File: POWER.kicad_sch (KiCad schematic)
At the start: 55 parts, among them J1 JST-PH 2-pin, U11 MAX17048G+, U13 BQ25895RTW, U23 LT3154AV#TRPBF, U24 TPS61023DRLR, U25 TPS2553DBVR

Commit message: finished annotation
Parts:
- removed U24: TPS61023DRLR, TPS61023:SOT563-ORI, symbol TPS61023DRLR:TPS61023DRLR
- added C21: 22u, symbol Device:C
- added U49: TPS61022, Package_DFN_QFN:Texas_RWU0007A_VQFN-7_2x2mm_P0.5mm, symbol Converter_DCDC:TPS61022
- renumbered C7 to C1, C14 to C10, C9 to C11, C15 to C12, C16 to C13, C12 to C14, C10 to C15, C8 to C16, C20 to C17, C21 to C18, C18 to C19, C5 to C2, C19 to C20, C17 to C22, C1 to C4, C2 to C5, C4 to C7, C11 to C8, C13 to C9, R5 to R1, R9 to R10, R6 to R11, R16 to R12, R17 to R13, R15 to R14, R14 to R15, R12 to R16, R13 to R17, R1 to R2, R4 to R3, R3 to R4, R2 to R5, R10 to R6, R11 to R7, R7 to R8, R8 to R9
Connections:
- net +5V_SYS: now also C21.2, U49.3 (VOUT)
- net BOOST_5V_EN: now also U49.5 (EN)
- net GND: now also C21.1, U49.1 (GND)
- net VSYS: now also U49.6 (MODE), U49.7 (VIN)
- net BST5V_FB renamed BOOST5V_FB
- net BOOST5V_FB: now also U49.4 (FB)
- net BST5V_SW renamed BOOST5V_SW
- net BOOST5V_SW: now also U49.2 (SW)
- net CHG_USB_DM: no longer names the net of U13.3 (D-)
- net CHG_USB_DP: no longer names the net of U13.2 (D+)
- net PMID renamed CHG_PMID
- net REGN renamed CHG_REGN
- net TS renamed CHG_TS
- net USB_ILIM renamed USB_HOST_ILIM
- net USB_MUX_SEL renamed CHG_DSEL_CFG
- no-connect marks 4 -> 6
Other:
- note added: "SWITCHABLE 5 V BOOST REGULATOR - TPS61022 VSYS TO +5V_SYS"
- note removed: "SWITCHABLE 5 V BOOST REGULATOR - TPS61023 VSYS TO +5V_SYS"
- title: (none) -> Power Input, Charging, Battery Monitoring and Regulated Rails
- moved on the sheet: C19, C2, C20, R14

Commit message: finished ANCHOR_DOCK sheet
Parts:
- removed C18: 120u, symbol Device:C
- removed J1: JST-PH 2-pin, symbol Connector_Generic:Conn_01x02
- added BT1: VTC-LP484594 3.7V 2200mAh protected battery pack, symbol Connector_Generic:Conn_01x03
- added C18: 120u, symbol Device:C_Polarized
- added J1: S3B-PH-SM4-TB(LF)(SN), Connector_JST:JST_PH_S3B-PH-SM4-TB_1x03-1MP_P2.00mm_Horizontal, symbol Connector_Generic:Conn_01x03
- C1: footprint (none) -> Capacitor_SMD:C_0603_1608Metric; DISTRIBUTOR_LINK (none) -> https://www.mouser.com/ProductDetail/Murata-Electronics/GRM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; MANUFACTURER (none) -> Murata; MPN (none) -> GRM188R71C105KA12D; Notes (none) -> N/A
- C10, C8, C9: footprint (none) -> Capacitor_SMD:C_1210_3225Metric; DISTRIBUTOR_LINK (none) -> https://www.mouser.com/ProductDetail/Murata-Electronics/GRM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; MANUFACTURER (none) -> Murata; MPN (none) -> GRM32ER71A476KE15L; Notes (none) -> Verify effective capacitance under DC bias.
- C11, C12, C19, C2, C20, C21, C4, C5: footprint (none) -> Capacitor_SMD:C_1206_3216Metric; DISTRIBUTOR_LINK (none) -> https://www.mouser.com/ProductDetail/Murata-Electronics/GRM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; MANUFACTURER (none) -> Murata; MPN (none) -> GRM31CR71A226KE15L; Notes (none) -> Verify effective capacitance under DC bias.
- C13: footprint (none) -> Capacitor_SMD:C_0603_1608Metric; DISTRIBUTOR_LINK (none) -> https://www.mouser.com/ProductDetail/Murata-Electronics/GRM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; MANUFACTURER (none) -> Murata; MPN (none) -> GRM188R71A225KE15D; Notes (none) -> N/A
- C14: footprint (none) -> Capacitor_SMD:C_0603_1608Metric; DISTRIBUTOR_LINK (none) -> https://www.mouser.com/ProductDetail/Murata-Electronics/GRM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; MANUFACTURER (none) -> Murata; MPN (none) -> GRM1885C1H100JA01D; Notes (none) -> N/A
- C15: footprint (none) -> Capacitor_SMD:C_0603_1608Metric; DISTRIBUTOR_LINK (none) -> https://www.mouser.com/ProductDetail/Murata-Electronics/GRM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; MANUFACTURER (none) -> Murata; MPN (none) -> GRM1885C1H102JA01D; Notes (none) -> N/A
- C16, C17: footprint (none) -> Capacitor_SMD:C_0603_1608Metric; DISTRIBUTOR_LINK (none) -> https://www.mouser.com/ProductDetail/Murata-Electronics/GRM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; MANUFACTURER (none) -> Murata; MPN (none) -> GRM188R71C104KA01D; Notes (none) -> N/A
- C22, C6: footprint (none) -> Capacitor_SMD:C_0805_2012Metric; DISTRIBUTOR_LINK (none) -> https://www.mouser.com/ProductDetail/Murata-Electronics/GRM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; MANUFACTURER (none) -> Murata; MPN (none) -> GRM21BR71A106KE51L; Notes (none) -> Verify effective capacitance under DC bias.
- C3: footprint (none) -> Capacitor_SMD:C_0603_1608Metric; DISTRIBUTOR_LINK (none) -> https://www.mouser.com/ProductDetail/Murata-Electronics/GRM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; MANUFACTURER (none) -> Murata; MPN (none) -> GRM188R71C473KA01D; Notes (none) -> N/A
- C7: footprint (none) -> Capacitor_SMD:C_0805_2012Metric; DISTRIBUTOR_LINK (none) -> https://www.mouser.com/ProductDetail/Murata-Electronics/GRM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; MANUFACTURER (none) -> Murata; MPN (none) -> GRM21BR71A475KA73L; Notes (none) -> Verify effective capacitance under DC bias.
- L1: footprint (none) -> Inductor_SMD:L_Wuerth_MAPI-4020; DISTRIBUTOR_LINK (none) -> https://www.mouser.com/ProductDetail/Wurth-Elektronik/74438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; MANUFACTURER (none) -> Wurth Elektronik; MPN (none) -> 74438356022; Notes (none) -> Verify charger thermal and layout.
- L2: footprint (none) -> Inductor_SMD:L_Wuerth_MAPI-4020; DISTRIBUTOR_LINK (none) -> https://www.mouser.com/ProductDetail/Wurth-Elektronik/74438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; MANUFACTURER (none) -> Wurth Elektronik; MPN (none) -> 744383560047HT; Notes (none) -> Verify peak current and switching frequency.
- L3: footprint (none) -> Inductor_SMD:L_Wuerth_HCI-5040; DISTRIBUTOR_LINK (none) -> https://www.mouser.com/ProductDetail/Wurth-Elektronik/74431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; MANUFACTURER (none) -> Wurth Elektronik; MPN (none) -> 744316100; Notes (none) -> Verify boost thermal and layout.
- NT1: DISTRIBUTOR_LINK (none) -> N/A; MANUFACTURER (none) -> PCB feature; MPN (none) -> N/A; Notes (none) -> N/A
- R1, R3: footprint (none) -> Resistor_SMD:R_0603_1608Metric; DISTRIBUTOR_LINK (none) -> https://www.mouser.com/ProductDetail/YAGEO/RC0603FR-0710KL?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; MANUFACTURER (none) -> Yageo; MPN (none) -> RC0603FR-0710KL; Notes (none) -> N/A
- R10: value 32.2k -> 32k4; footprint (none) -> Resistor_SMD:R_0603_1608Metric; DISTRIBUTOR_LINK (none) -> https://www.mouser.co.il/en/ProductDetail/YAGEO/RC0603FR-07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; MANUFACTURER (none) -> Yageo; MPN (none) -> RC0603FR-0732K4L
- R11: footprint (none) -> Resistor_SMD:R_0603_1608Metric; DISTRIBUTOR_LINK (none) -> https://www.mouser.com/ProductDetail/YAGEO/RC0603FR-0740K2L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; MANUFACTURER (none) -> Yageo; MPN (none) -> RC0603FR-0740K2L; Notes (none) -> N/A
- R12, R13, R15, R17, R7, R9: footprint (none) -> Resistor_SMD:R_0603_1608Metric; DISTRIBUTOR_LINK (none) -> https://www.mouser.com/ProductDetail/YAGEO/RC0603FR-07100KL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; MANUFACTURER (none) -> Yageo; MPN (none) -> RC0603FR-07100KL; Notes (none) -> N/A
- R14: footprint (none) -> Resistor_SMD:R_0603_1608Metric; DISTRIBUTOR_LINK (none) -> https://www.mouser.com/ProductDetail/YAGEO/RC0603FR-0743K2L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; MANUFACTURER (none) -> Yageo; MPN (none) -> RC0603FR-0743K2L; Notes (none) -> N/A
- R16: footprint (none) -> Resistor_SMD:R_0603_1608Metric; DISTRIBUTOR_LINK (none) -> https://www.mouser.com/ProductDetail/YAGEO/RC0603FR-07732KL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; MANUFACTURER (none) -> Yageo; MPN (none) -> RC0603FR-07732KL; Notes (none) -> N/A
- R2: value 260R -> 261R; footprint (none) -> Resistor_SMD:R_0603_1608Metric; DISTRIBUTOR_LINK (none) -> https://www.mouser.com/en/ProductDetail/YAGEO/AF0603FR-0726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; MANUFACTURER (none) -> Yageo; MPN (none) -> AF0603FR-07261RL
- R4: value 10k -> 5k23; footprint (none) -> Resistor_SMD:R_0603_1608Metric; DISTRIBUTOR_LINK (none) -> https://eu.mouser.com/en/ProductDetail/YAGEO/RC0603FR-075K2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; MANUFACTURER (none) -> Yageo; MPN (none) -> RC0603FR-075K23L; Notes (none) -> N/A
- R5: value 10k -> 30k1; footprint (none) -> Resistor_SMD:R_0603_1608Metric; DISTRIBUTOR_LINK (none) -> https://eu.mouser.com/en/ProductDetail/YAGEO/RC0603FR-0730K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; MANUFACTURER (none) -> Yageo; MPN (none) -> RC0603FR-0730K1L; Notes (none) -> N/A
- R6: footprint (none) -> Resistor_SMD:R_0603_1608Metric; DISTRIBUTOR_LINK (none) -> https://www.mouser.com/ProductDetail/YAGEO/RC0603FR-07121KL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; MANUFACTURER (none) -> Yageo; MPN (none) -> RC0603FR-07121KL; Notes (none) -> N/A
- R8: footprint (none) -> Resistor_SMD:R_0603_1608Metric; DISTRIBUTOR_LINK (none) -> https://www.mouser.com/ProductDetail/YAGEO/RC0603FR-07232KL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; MANUFACTURER (none) -> Yageo; MPN (none) -> RC0603FR-07232KL; Notes (none) -> N/A
- TP1, TP2, TP3, TP4, TP5, TP6, TP7: footprint (none) -> TestPoint:TestPoint_Pad_D1.5mm; DISTRIBUTOR_LINK (none) -> N/A; MANUFACTURER (none) -> PCB feature; MPN (none) -> N/A; Notes (none) -> N/A; now left out of the parts list
- U11: DISTRIBUTOR_LINK (none) -> https://www.mouser.com/ProductDetail/Analog-Devices-Maxim-I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; MANUFACTURER (none) -> Analog Devices; MPN (none) -> MAX17048G+T10; Notes (none) -> Confirm battery profile assumptions.
- U13: DISTRIBUTOR_LINK (none) -> https://www.mouser.com/ProductDetail/Texas-Instruments/BQ25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; MANUFACTURER (none) -> Texas Instruments; MPN (none) -> BQ25895RTWR; Notes (none) -> Assembly: exposed pad, thermal vias and X-ray.
- U23: DISTRIBUTOR_LINK (none) -> https://www.mouser.com/ProductDetail/Analog-Devices/LT3154A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; MPN (none) -> LT3154AV#TRPBF; Notes (none) -> SOURCING: non-stocked/long lead; obtain PCBWay quote.
- U25: DISTRIBUTOR_LINK (none) -> https://www.mouser.com/ProductDetail/Texas-Instruments/TPS2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; MANUFACTURER (none) -> Texas Instruments; MPN (none) -> TPS2553DBVR; Notes (none) -> N/A
- U49: DISTRIBUTOR_LINK (none) -> https://www.mouser.com/ProductDetail/Texas-Instruments/TPS6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; MANUFACTURER (none) -> Texas Instruments; MPN (none) -> TPS61022RWUR; Notes (none) -> Assembly: EP ground/X-ray; verify peak current/thermal.
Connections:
- net CHG_TS: now also J1.2 (Pin_2)
- net GND: now also C18.2, J1.3 (Pin_3)
- net VBAT: now also J1.1 (Pin_1)
- net VBUS_HOST: now also C18.1
- no-connect marks 6 -> 9

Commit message: the schematic is finished
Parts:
- R10, R2: Notes (none) -> N/A
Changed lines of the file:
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@@
 			)
 		)
-		(property "Notes" ""
+		(property "Notes" "N/A"
 			(at 35.56 69.85 90)
 			(hide yes)
@@
 			)
 		)
-		(property "Notes" ""
+		(property "Notes" "N/A"
 			(at 38.1 168.91 0)
 			(hide yes)

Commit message: finished schematic phase
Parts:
- C18: footprint (none) -> FOBtool_Custom:CP_Panasonic_EEF-TX_7.3x4.3mm
- NT1: footprint (none) -> FOBtool_Custom:NetTie_2_SMD_3.0mm_Current
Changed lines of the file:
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@@
 		(in_bom no)
 		(on_board yes)
-		(in_pos_files yes)
+		(in_pos_files no)
 		(dnp no)
 		(fields_autoplaced yes)
@@
 			)
 		)
-		(property "Footprint" ""
+		(property "Footprint" "FOBtool_Custom:NetTie_2_SMD_3.0mm_Current"
 			(at 33.02 86.36 0)
 			(hide yes)
@@
 			)
 		)
-		(property "Footprint" ""
+		(property "Footprint" "FOBtool_Custom:CP_Panasonic_EEF-TX_7.3x4.3mm"
 			(at 254.9652 88.9 0)
 			(hide yes)

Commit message: adding 3d models
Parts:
- J1: symbol Connector_Generic:Conn_01x03 -> FOBtool_Custom:JST_PH_3Pin_MP
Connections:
- no-connect marks 9 -> 10
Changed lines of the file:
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@@
 	)
 	(no_connect
+		(at 123.19 83.82)
+	)
+	(no_connect
 		(at 53.34 64.77)
 	)
@@
 	)
 	(symbol
-		(lib_id "Connector_Generic:Conn_01x03")
+		(lib_id "FOBtool_Custom:JST_PH_3Pin_MP")
 		(at 118.11 81.28 0)
 		(unit 1)
@@
 		(pin "2"
 		)
+		(pin "MP"
+		)
 		(instances

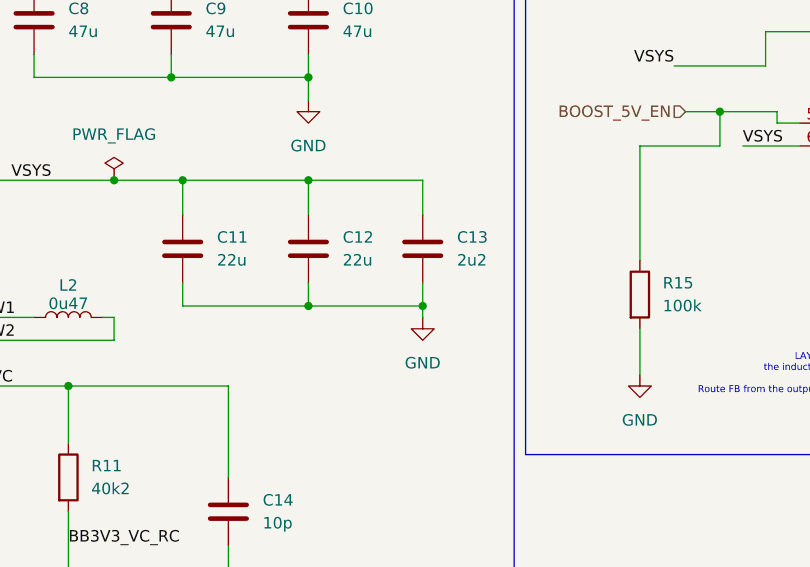
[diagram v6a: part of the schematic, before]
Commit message: changiong bootsel buttom in rp
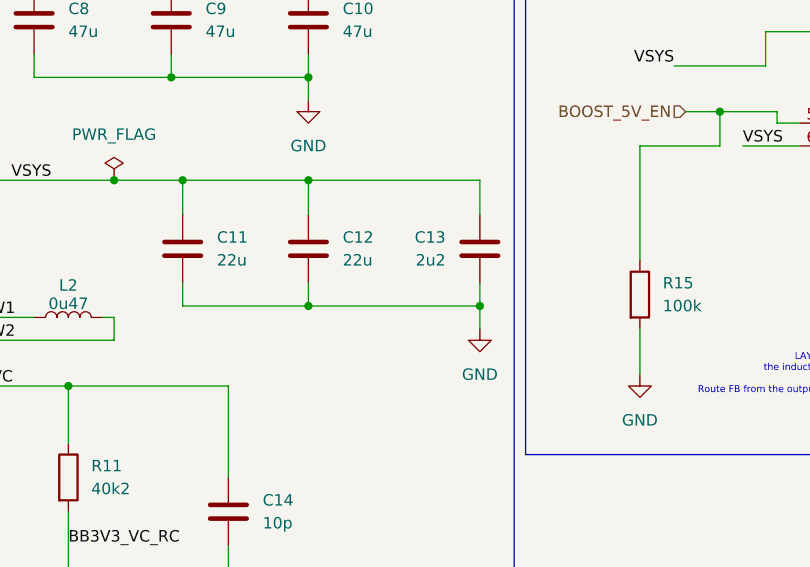
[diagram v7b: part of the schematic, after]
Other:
- moved on the sheet: C13
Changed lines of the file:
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@@
 	)
 	(junction
-		(at 140.97 148.59)
+		(at 140.97 134.62)
 		(diameter 0)
 		(color 0 0 0 0)
@@
 	)
 	(junction
+		(at 160.02 148.59)
+		(diameter 0)
+		(color 0 0 0 0)
+	)
+	(junction
 		(at 242.57 105.41)
 		(diameter 0)
@@
 	)
 	(junction
-		(at 153.67 148.59)
-		(diameter 0)
-		(color 0 0 0 0)
-	)
-	(junction
 		(at 99.06 134.62)
 		(diameter 0)
@@
 	)
 	(junction
-		(at 224.79 24.13)
+		(at 140.97 148.59)
 		(diameter 0)
 		(color 0 0 0 0)
 	)
 	(junction
-		(at 119.38 134.62)
+		(at 224.79 24.13)
 		(diameter 0)
 		(color 0 0 0 0)
 	)
 	(junction
-		(at 129.54 59.69)
+		(at 119.38 134.62)
 		(diameter 0)
 		(color 0 0 0 0)
 	)
 	(junction
-		(at 20.32 162.56)
+		(at 129.54 59.69)
 		(diameter 0)
 		(color 0 0 0 0)
 	)
 	(junction
-		(at 140.97 134.62)
+		(at 20.32 162.56)
 		(diameter 0)
 		(color 0 0 0 0)
@@
 	(wire
 		(pts
-			(xy 153.67 148.59) (xy 140.97 148.59)
+			(xy 140.97 148.59) (xy 160.02 148.59)
 		)
 		(stroke
@@
 	(wire
 		(pts
-			(xy 153.67 148.59) (xy 153.67 149.86)
+			(xy 160.02 148.59) (xy 160.02 151.13)
 		)
 		(stroke
@@
 	(wire
 		(pts
-			(xy 153.67 146.05) (xy 153.67 148.59)
+			(xy 160.02 146.05) (xy 160.02 148.59)
 		)
 		(stroke
@@
 	(wire
 		(pts
-			(xy 153.67 138.43) (xy 153.67 134.62)
+			(xy 160.02 138.43) (xy 160.02 134.62)
 		)
 		(stroke
@@
 	(wire
 		(pts
-			(xy 140.97 134.62) (xy 153.67 134.62)
+			(xy 140.97 134.62) (xy 160.02 134.62)
 		)
 		(stroke
@@
 	(symbol
 		(lib_id "Device:C")
-		(at 153.67 142.24 0)
+		(at 160.02 142.24 0)
+		(mirror y)
 		(unit 1)
 		(body_style 1)
@@
 		(in_pos_files yes)
 		(dnp no)
-		(fields_autoplaced yes)
 		(property "Reference" "C13"
-			(at 157.48 140.9699 0)
+			(at 156.21 140.9699 0)
 			(show_name no)
 			(do_not_autoplace no)
@@
 		)
 		(property "Value" "2u2"
-			(at 157.48 143.5099 0)
+			(at 156.21 143.5099 0)
 			(show_name no)
 			(do_not_autoplace no)
@@
 		)
 		(property "Footprint" "Capacitor_SMD:C_0603_1608Metric"
-			(at 154.6352 146.05 0)
+			(at 159.0548 146.05 0)
 			(hide yes)
 			(show_name no)
@@
 		)
 		(property "Datasheet" "https://pim.murata.com/en-global/pim/details/?partNum=GRM188R71A225KE15D"
-			(at 153.67 142.24 0)
+			(at 160.02 142.24 0)
 			(hide yes)
 			(show_name no)
@@
 		)
 		(property "Description" "Unpolarized capacitor"
-			(at 153.67 142.24 0)
+			(at 160.02 142.24 0)
 			(hide yes)
 			(show_name no)
@@
 		)
 		(property "DISTRIBUTOR_LINK" "https://www.mouser.com/ProductDetail/Murata-Electronics/GRM188R71A225KE15D?qs=FI%2F1jqMWe7rgTInCPAq47w%3D%3D"
-			(at 153.67 142.24 0)
+			(at 160.02 142.24 0)
 			(hide yes)
 			(show_name no)
@@
 		)
 		(property "MPN" "GRM188R71A225KE15D"
-			(at 153.67 142.24 0)
+			(at 160.02 142.24 0)
 			(hide yes)
 			(show_name no)
@@
 		)
 		(property "KLC_S3.3" ""
-			(at 153.67 142.24 0)
+			(at 160.02 142.24 0)
 			(hide yes)
 			(show_name no)
@@
 		)
 		(property "KLC_S4.1" ""
-			(at 153.67 142.24 0)
+			(at 160.02 142.24 0)
 			(hide yes)
 			(show_name no)
@@
 		)
 		(property "KLC_S4.2_DVDD" ""
-			(at 153.67 142.24 0)
+			(at 160.02 142.24 0)
 			(hide yes)
 			(show_name no)
@@
 		)
 		(property "KLC_S4.2_VREG_LX" ""
-			(at 153.67 142.24 0)
+			(at 160.02 142.24 0)
 			(hide yes)
 			(show_name no)
@@
 		)
 		(property "Notes" "N/A"
-			(at 153.67 142.24 0)
+			(at 160.02 142.24 0)
 			(hide yes)
 			(show_name no)
@@
 		)
 		(property "MANUFACTURER" "Murata"
-			(at 153.67 142.24 0)
+			(at 160.02 142.24 0)
 			(hide yes)
 			(show_name no)
@@
 		)
 		(property "TUNING_ALTERNATIVES" ""
-			(at 153.67 142.24 0)
+			(at 160.02 142.24 0)
 			(hide yes)
 			(show_name no)
@@
 	(symbol
 		(lib_id "power:GND")
-		(at 153.67 149.86 0)
+		(at 160.02 151.13 0)
 		(unit 1)
 		(body_style 1)
@@
 		(fields_autoplaced yes)
 		(property "Reference" "#PWR015"
-			(at 153.67 156.21 0)
+			(at 160.02 157.48 0)
 			(hide yes)
 			(show_name no)
@@
 		)
 		(property "Value" "GND"
-			(at 153.67 154.94 0)
+			(at 160.02 156.21 0)
 			(show_name no)
 			(do_not_autoplace no)
@@
 		)
 		(property "Footprint" ""
-			(at 153.67 149.86 0)
+			(at 160.02 151.13 0)
 			(hide yes)
 			(show_name no)
@@
 		)
 		(property "Datasheet" ""
-			(at 153.67 149.86 0)
+			(at 160.02 151.13 0)
 			(hide yes)
 			(show_name no)
@@
 		)
 		(property "Description" "Power symbol creates a global label with name \"GND\" , ground"
-			(at 153.67 149.86 0)
+			(at 160.02 151.13 0)
 			(hide yes)
 			(show_name no)
